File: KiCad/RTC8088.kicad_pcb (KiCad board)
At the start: 2 copper layers, 86.4 x 38.1 mm, 11 parts, among them SW1 Address Select, U1 DS12885, U2 ATF16V8B, Y1 32768Hz

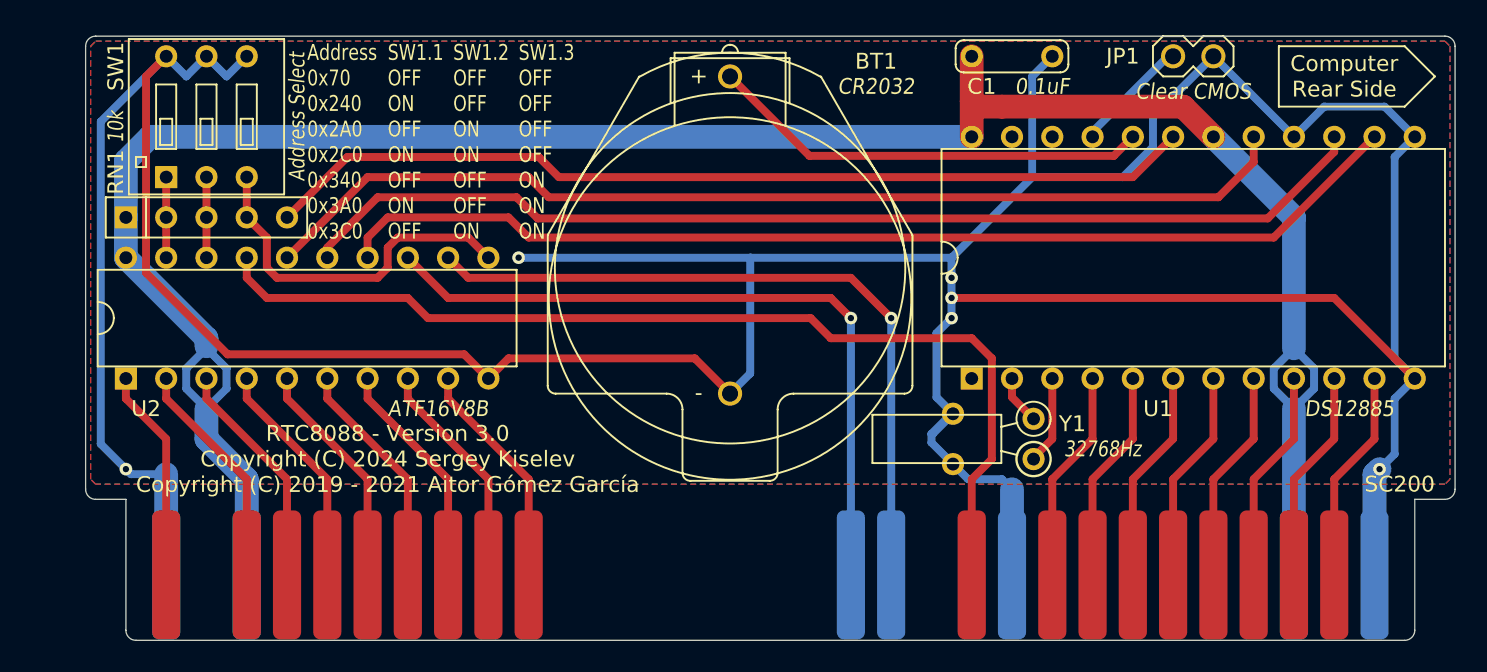
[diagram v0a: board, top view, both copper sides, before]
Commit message: Replace tht DS12855 with smt bq3285
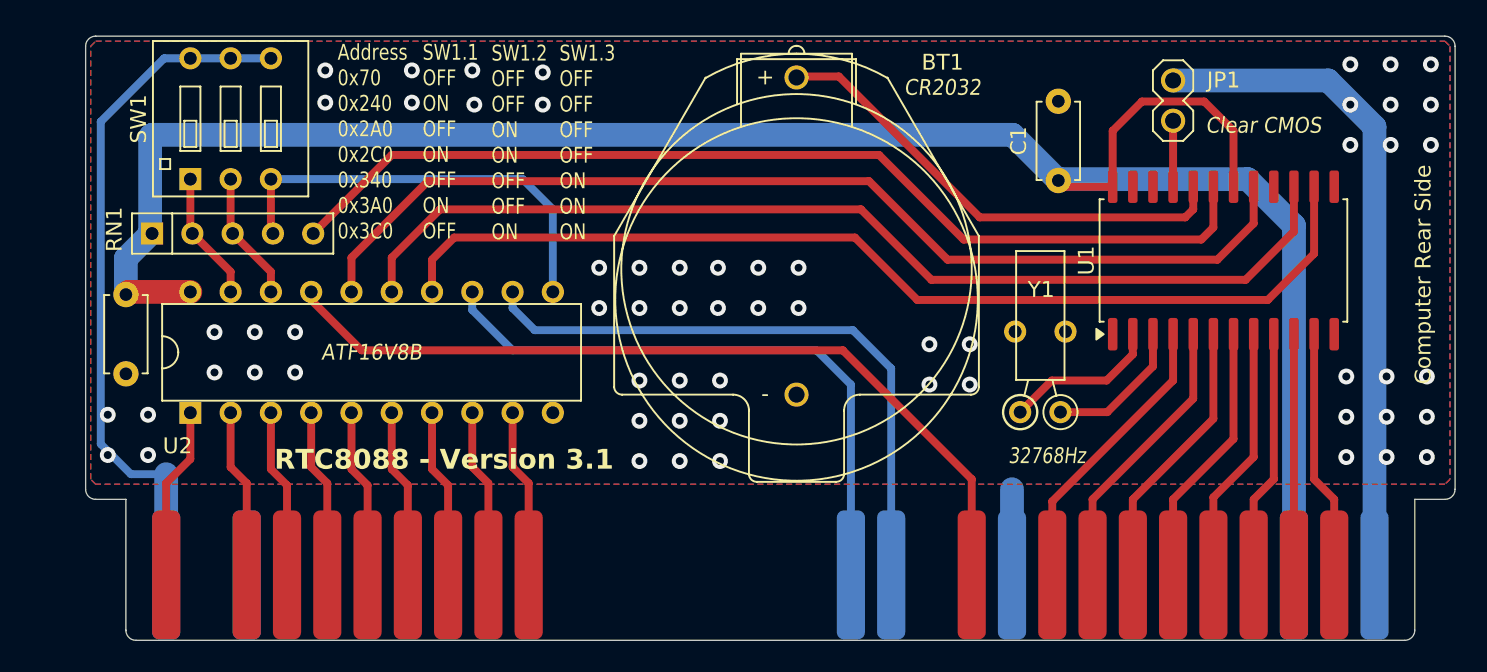
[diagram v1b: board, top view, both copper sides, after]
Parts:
- added C2: 0.1uF, Capacitor_THT:C_Disc_D4.7mm_W2.5mm_P5.00mm, F.Cu at (111.8, 73.4)
- C1: footprint My_Components:Cap_Cer_508 -> Capacitor_THT:C_Disc_D4.7mm_W2.5mm_P5.00mm
- U1: footprint My_Components:IC_DIP24_600 -> Package_SO:SOIC-24W_7.5x15.4mm_P1.27mm
- moved REF** 24.7 mm to (148.8, 66.0)
- moved REF** 22.9 mm to (134.1, 65.9)
- moved C1 8.36 mm to (170.6, 66.3), turned to 90 degrees
- moved U2 4.60 mm to (127.3, 77.1)
- moved BT1 4.19 mm to (154.1, 73.8)
- moved JP1 3.07 mm to (177.8, 61.2), turned to 90 degrees
- moved RN1 1.94 mm to (118.5, 69.6)
- moved U1 1.91 mm to (181.0, 71.3), turned to 90 degrees
- moved Y1 1.74 mm to (169.4, 80.9), turned to 180 degrees
- moved SW1 1.53 mm to (118.4, 62.4)
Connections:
- U1 pad 2: Net-(U1-Pad2) -> Net-(U1-X1)
- U1 pad 3: Net-(U1-Pad3) -> Net-(U1-X2)
- Y1 pad 1: Net-(U1-Pad2) -> Net-(U1-X2)
- Y1 pad 2: Net-(U1-Pad3) -> Net-(U1-X1)
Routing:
- net GND: track 271.3 -> 91.5 mm, vias 6 -> 61
- net VCC: track 145.9 -> 131.2 mm
- net /AEN: track 64.2 -> 52.6 mm
- net Net-(U1-X1): track 0.00 -> 10.4 mm
- net Net-(U1-X2): track 0.00 -> 9.06 mm
- net /IOR: track 45.4 -> 38.6 mm, vias 1 -> 0
- net /IOW: track 45.4 -> 39.2 mm, vias 1 -> 0
- net Net-(U1-Pad3): track 5.61 -> 0.00 mm
- net /D0: track 13.1 -> 18.3 mm
- net /~{IRQ}: track 59.0 -> 63.9 mm
- net /D1: track 13.1 -> 17.9 mm
- net /AS2: track 22.8 -> 27.3 mm
- net /D2: track 13.1 -> 17.3 mm
- net /A8: track 14.2 -> 10.3 mm
- net /A6: track 14.2 -> 10.3 mm
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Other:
- board text added: "Copyright (C) 2026 [zyga64] Copyright (C) 2024 Sergey Kiselev Copyright (C) 2019 - 2021 Aitor Gómez García"
- board text added: "RTC8088 - Version 3.1"
- board text added: "https://github.com/zyga64/RTC8088"
- board text removed: "Based on the previous work: Sergey Kiselev - Xi 8088 Aitor Gómez García - RTC8088 Dr. Scott M. Baker - 8-bit ISA DiskOnChip / RTC board"
- board text removed: "Copyright (C) 2024 Sergey Kiselev Copyright (C) 2019 - 2021 Aitor Gómez García Design files and documentation: https://github.com/spark2k06/RTC8088 Licensed under CERN-OHL-S: https://cern-ohl.web.cern.ch"
- board text removed: "RTC8088 - Version 3.0"
- board text removed: "RTC8088 - Version 3.0 Copyright (C) 2024 Sergey Kiselev Copyright (C) 2019 - 2021 Aitor Gómez García"
- board text removed: "SC200"
- board text removed: "aitorgomez.net"
- board text removed: "www.malinov.com"
